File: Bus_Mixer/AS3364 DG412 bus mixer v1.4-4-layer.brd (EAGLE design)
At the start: 84.8 x 52.5 mm, 145 parts, among them IC1 PCA9539PW, IC10 DG412-J, IC11 DG412-J, IC2 TL074JT, IC3 TL072JT, IC4 TL074JT, IC6 TL072JT, IC7 TL074JT, IC8 DG412-J, IC9 DG412-J

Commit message: Lots of vias
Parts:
- moved C5 0.48 mm to (34.1, 17.1), turned to 0 degrees
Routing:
- net OUT4: track 30.8 -> 33.0 mm
- net +12V: track 245.8 -> 247.3 mm
- net OUT5: track 30.4 -> 31.3 mm
- net N$35: track 8.07 -> 8.67 mm
- net N$36: track 9.36 -> 9.95 mm
- net SUM_A: track 39.1 -> 38.5 mm
- net +3V3: track 51.4 -> 51.9 mm
- net N$38: track 10.7 -> 11.2 mm
- net DIG_6_BUS_B: track 43.4 -> 42.9 mm
- net GND: track 69.1 -> 69.3 mm, vias 63 -> 121

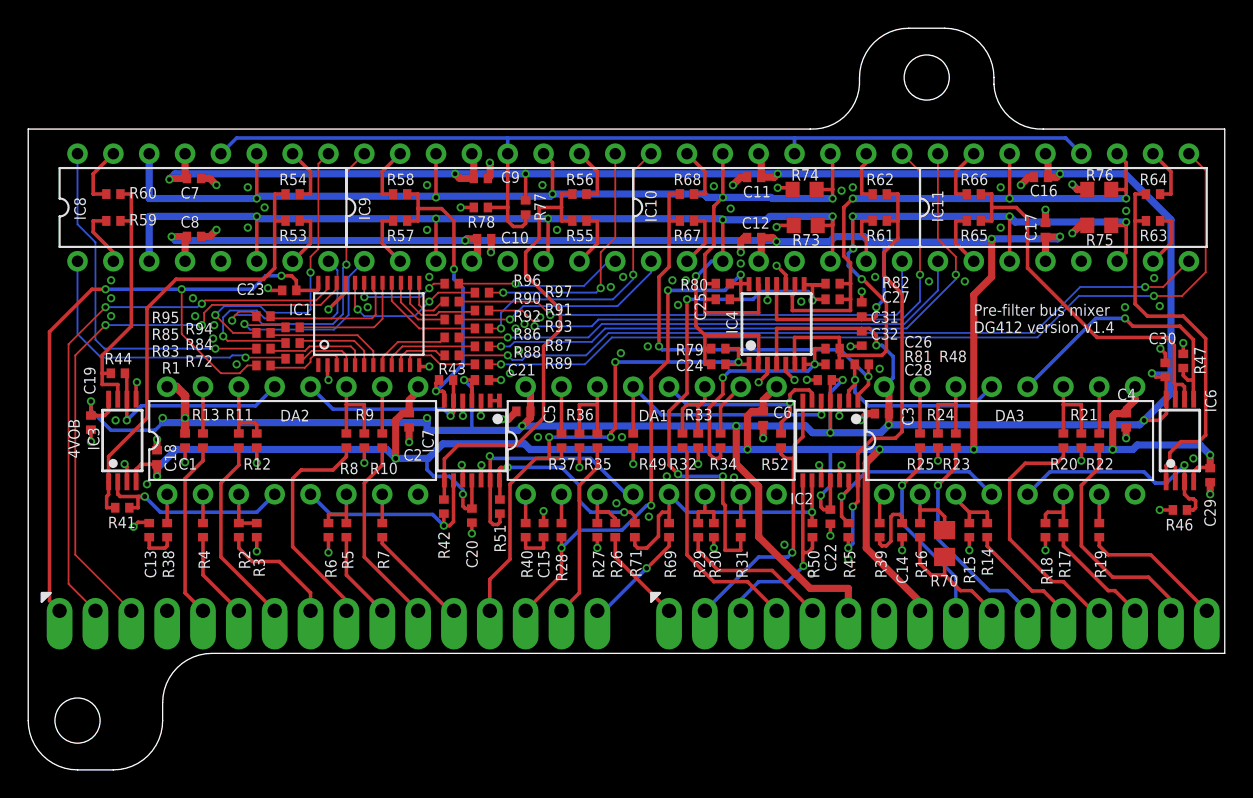
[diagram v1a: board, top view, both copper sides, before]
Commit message: Finished v1.4 4 layer
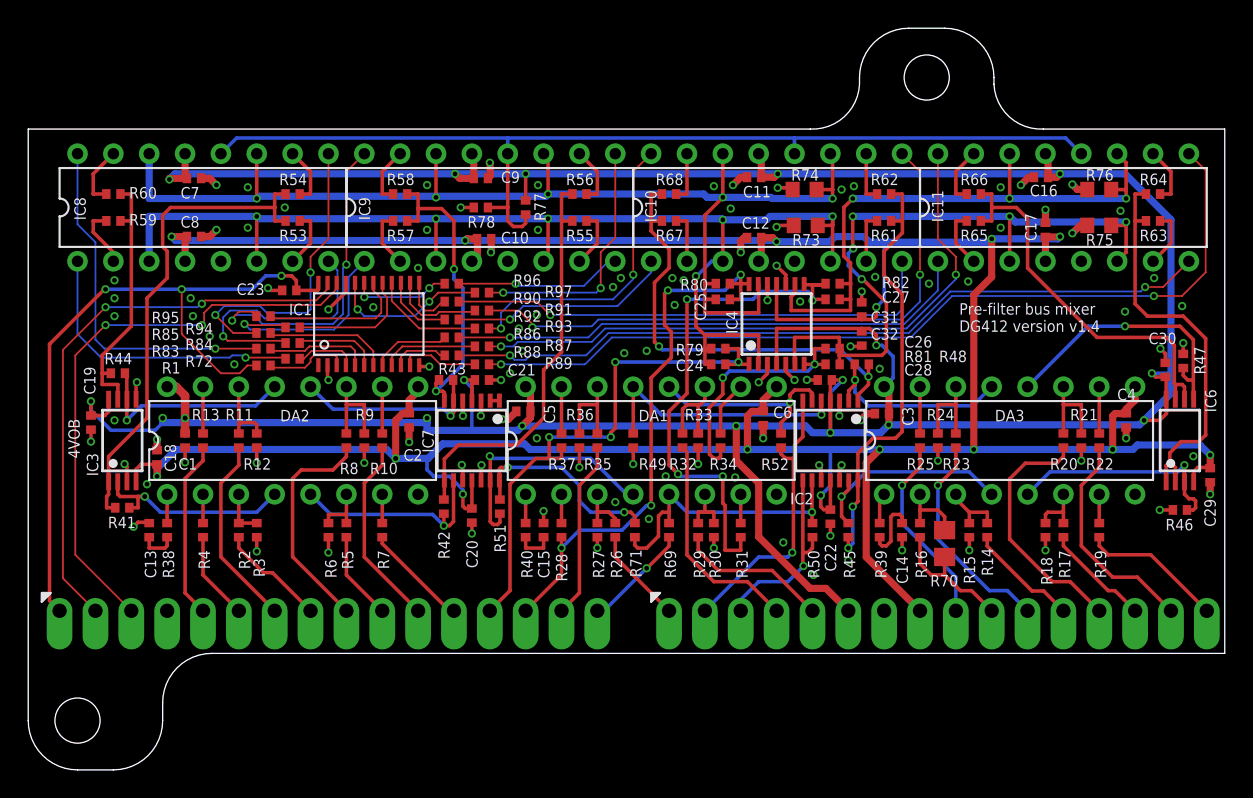
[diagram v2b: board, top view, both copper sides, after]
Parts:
- moved R67 1.27 mm to (44.5, 30.6)
- moved R68 1.27 mm to (44.5, 32.5)
- moved R61 0.32 mm to (59.7, 30.6)
- moved R62 0.32 mm to (59.7, 32.5)
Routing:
- net OUT4: track 33.0 -> 29.1 mm
- net OUT2: track 32.9 -> 34.8 mm
- net +12V: track 247.3 -> 246.3 mm
- net OUT5: track 31.3 -> 32.0 mm
- net CV2: track 8.44 -> 7.69 mm
- net N$4: track 16.8 -> 16.2 mm
- net SW5B: track 4.15 -> 3.63 mm
- net SW5A: track 4.15 -> 3.63 mm
- net +3V3: track 51.9 -> 51.4 mm
- net GND: vias 121 -> 117

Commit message: Routed chain inverter
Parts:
- added JP1: JUMPER-SMT_2_NC_TRACE_SILK-DNM, SparkFun-Jumpers:SMT-JUMPER_2_NC_TRACE_SILK
- added JP4: JUMPER-SMT_2_NO_SILK-DNM, SparkFun-Jumpers:SMT-JUMPER_2_NO_SILK
- added R98, R99: 47k, rcl:R0402
- moved R42 2.26 mm to (28.1, 8.18)
- moved R51 2.22 mm to (32.5, 8.18)
- moved C20 1.59 mm to (30.5, 8.18)
- moved IC7 1.59 mm to (30.5, 13.5)
- moved C21 1.53 mm to (29.8, 18.7), turned to 270 degrees
- moved R43 0.35 mm to (28.5, 19.1), turned to 90 degrees
- moved C5 0.24 mm to (34.4, 17.1)
- moved R89 0.08 mm to (31.2, 20.6)
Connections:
- new net N$44: IC7.2, R98.2, R99.1
- new net SVF_CHAIN_SELECTED: JP1.2, JP4.2, R69.2
- net N$22: now also JP4.1, R98.1; no longer IC7.2
- net SVF_CHAIN: now also JP1.1, R99.2; no longer R69.2
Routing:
- net SVF_CHAIN: track 7.61 -> 25.5 mm, vias 1 -> 2
- net N$22: track 0.65 -> 16.5 mm, vias 0 -> 1
- net SVF_CHAIN_SELECTED: track 0.00 -> 12.3 mm, vias 0 -> 1
- net -12V: track 234.7 -> 238.4 mm
- net N$17: track 17.4 -> 20.7 mm
- net CON3: track 13.4 -> 16.4 mm
- net N$44: track 0.00 -> 2.44 mm
- net GND: track 69.3 -> 71.6 mm
- net N$20: track 14.4 -> 12.3 mm
- net OUT4: track 29.1 -> 30.7 mm
- net +12V: track 246.3 -> 247.9 mm, vias 18 -> 17
- net CON4: track 14.9 -> 16.3 mm
- net CV_A_DRY: track 12.6 -> 13.3 mm
- net OUT3: track 21.5 -> 22.2 mm
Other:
- board text added: "S B"
- board text removed: "SUM B"
